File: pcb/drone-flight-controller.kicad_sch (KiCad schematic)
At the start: 88 parts, among them J1 SWD, J10 CONN_MANDO, J11 OLED, J12 STM32 SPI, J13 STM32 I2C, J14 STM32 USART, J2 Jumper, J3 USB_B_Micro, J4 CONN_MOT_1, J5 CONN_MOT_2, J6 CONN_MOT_3, J7 CONN_MOT_4, J8 XT-60, J9 LIDAR, SW1 TC-6610_C7528713, SW2 TC-6610_C7528713, SW4 SS12D10G5_C7431054, U1 STM32F103R8T6, U10 LM7805_TO220, U11 AMS1117-3.3, U2 MPU-6050, Y1 8MHz, Y2 32.768KHz

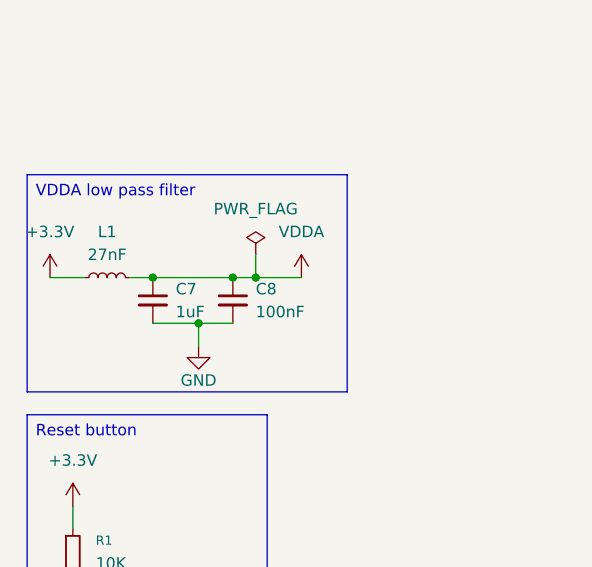
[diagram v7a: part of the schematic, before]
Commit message: pcb: layout session state
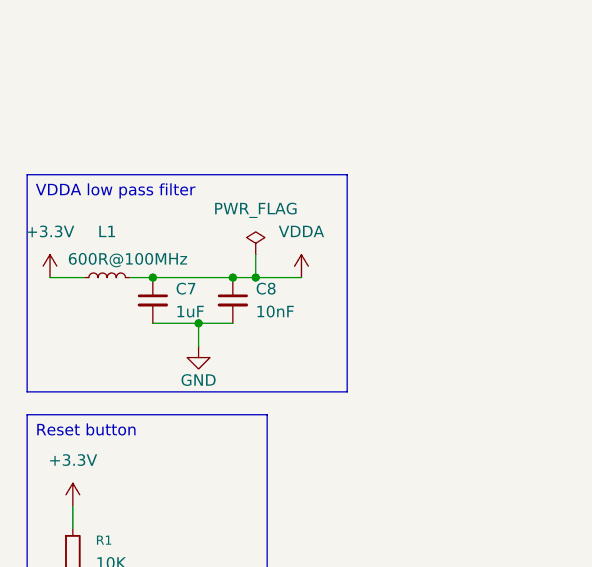
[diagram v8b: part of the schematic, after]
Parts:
- C8: value 100nF -> 10nF
- L1: value 27nF -> 600R@100MHz
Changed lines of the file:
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@@
 		(in_pos_files yes)
 		(dnp no)
-		(fields_autoplaced yes)
 		(property "Reference" "L1"
 			(at 25.4 152.4 90)
@@
 			)
 		)
-		(property "Value" "27nF"
-			(at 25.4 154.94 90)
+		(property "Value" "600R@100MHz"
+			(at 27.686 155.448 90)
 			(show_name no)
 			(do_not_autoplace no)
@@
 			)
 		)
-		(property "Value" "100nF"
+		(property "Value" "10nF"
 			(at 41.91 161.2962 0)
 			(show_name no)
@@
 			)
 		)
-    (property "LCSC" "C7431054" (at 38.1 50.8 0)
-      (effects (font (size 1.27 1.27)) (hide yes))
-    )
-    (property "Part" "SS12D10G5" (at 38.1 50.8 0)
-      (effects (font (size 1.27 1.27)) (hide yes))
-    )
-    (property "Manufacturer" "SHOU HAN" (at 38.1 50.8 0)
-      (effects (font (size 1.27 1.27)) (hide yes))
-    )
+		(property "LCSC" "C7431054"
+			(at 38.1 50.8 0)
+			(hide yes)
+			(show_name no)
+			(do_not_autoplace no)
+			(effects
+				(font
+					(size 1.27 1.27)
+				)
+			)
+		)
+		(property "Part" "SS12D10G5"
+			(at 38.1 50.8 0)
+			(hide yes)
+			(show_name no)
+			(do_not_autoplace no)
+			(effects
+				(font
+					(size 1.27 1.27)
+				)
+			)
+		)
+		(property "Manufacturer" "SHOU HAN"
+			(at 38.1 50.8 0)
+			(hide yes)
+			(show_name no)
+			(do_not_autoplace no)
+			(effects
+				(font
+					(size 1.27 1.27)
+				)
+			)
+		)
 		(pin "1"
 		)
